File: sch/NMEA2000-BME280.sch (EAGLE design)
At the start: 5 parts, among them IC1 5V

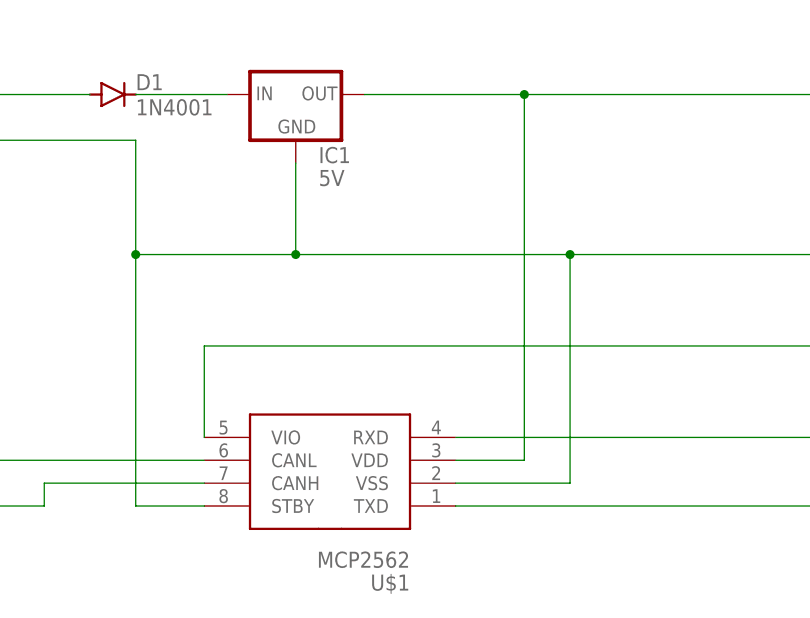
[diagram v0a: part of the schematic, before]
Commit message: added some missing values
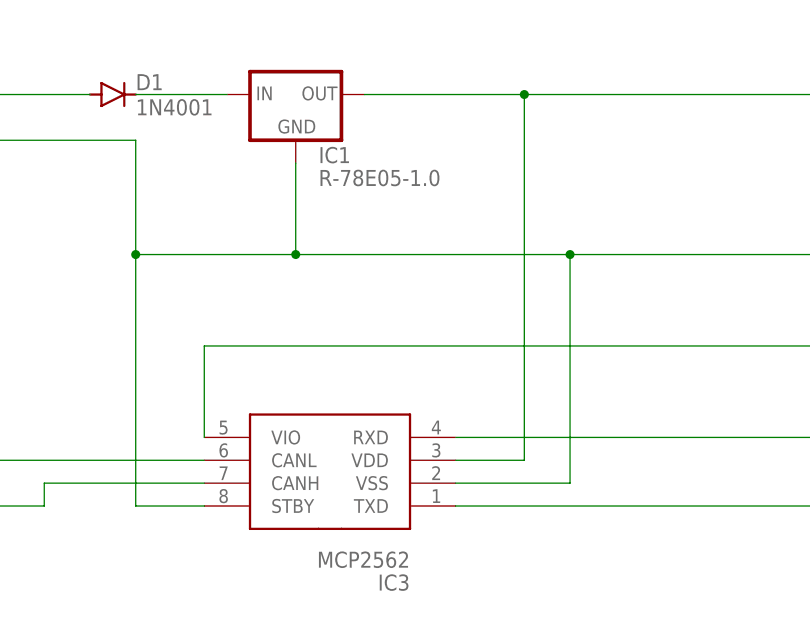
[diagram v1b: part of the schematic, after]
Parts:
- IC1: value 5V -> R-78E05-1.0
- renumbered U$1 to IC3
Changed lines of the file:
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@@
 <parts>
 <part name="ESP1" library="_esp32" deviceset="ESP32-NODEMCU" device="" value="ESP32 NodeMCU"/>
-<part name="IC1" library="v-reg" library_urn="urn:adsk.eagle:library:409" deviceset="78XXS" device="" package3d_urn="urn:adsk.eagle:package:30342/1" value="5V"/>
-<part name="U$1" library="_eigene" deviceset="MCP2562" device=""/>
+<part name="IC1" library="v-reg" library_urn="urn:adsk.eagle:library:409" deviceset="78XXS" device="" package3d_urn="urn:adsk.eagle:package:30342/1" value="R-78E05-1.0"/>
+<part name="IC3" library="_eigene" deviceset="MCP2562" device=""/>
 <part name="FRAME1" library="frames" library_urn="urn:adsk.eagle:library:229" deviceset="DINA4_L" device=""/>
 <part name="D1" library="diode" library_urn="urn:adsk.eagle:library:210" deviceset="1N4004" device="" package3d_urn="urn:adsk.eagle:package:43336/1" value="1N4001"/>
@@
 <attribute name="VALUE" x="81.28" y="83.82" size="1.778" layer="96"/>
 </instance>
-<instance part="U$1" gate="G$1" x="81.28" y="68.58" smashed="yes" rot="R180">
+<instance part="IC3" gate="G$1" x="81.28" y="68.58" smashed="yes" rot="R180">
 <attribute name="NAME" x="91.44" y="40.64" size="1.778" layer="95" rot="R180"/>
 <attribute name="VALUE" x="91.44" y="43.18" size="1.778" layer="96" rot="R180"/>
@@
 <segment>
 <wire x1="223.52" y1="109.22" x2="223.52" y2="55.88" width="0.1524" layer="91"/>
-<pinref part="U$1" gate="G$1" pin="RXD"/>
+<pinref part="IC3" gate="G$1" pin="RXD"/>
 <wire x1="223.52" y1="55.88" x2="96.52" y2="55.88" width="0.1524" layer="91"/>
 <pinref part="ESP1" gate="G$1" pin="GPIO4"/>
@@
 <net name="N$2" class="0">
 <segment>
-<pinref part="U$1" gate="G$1" pin="TXD"/>
+<pinref part="IC3" gate="G$1" pin="TXD"/>
 <wire x1="96.52" y1="48.26" x2="226.06" y2="48.26" width="0.1524" layer="91"/>
 <wire x1="226.06" y1="48.26" x2="226.06" y2="116.84" width="0.1524" layer="91"/>
@@
 <pinref part="IC1" gate="1" pin="OUT"/>
 <wire x1="162.56" y1="93.98" x2="104.14" y2="93.98" width="0.1524" layer="91"/>
-<pinref part="U$1" gate="G$1" pin="VDD"/>
+<pinref part="IC3" gate="G$1" pin="VDD"/>
 <wire x1="104.14" y1="93.98" x2="86.36" y2="93.98" width="0.1524" layer="91"/>
 <wire x1="96.52" y1="53.34" x2="104.14" y2="53.34" width="0.1524" layer="91"/>
@@
 <pinref part="ESP1" gate="G$1" pin="GND1"/>
 <wire x1="144.78" y1="106.68" x2="162.56" y2="106.68" width="0.1524" layer="91"/>
-<pinref part="U$1" gate="G$1" pin="VSS"/>
+<pinref part="IC3" gate="G$1" pin="VSS"/>
 <wire x1="96.52" y1="50.8" x2="109.22" y2="50.8" width="0.1524" layer="91"/>
 <wire x1="109.22" y1="50.8" x2="109.22" y2="76.2" width="0.1524" layer="91"/>
 <junction x="109.22" y="76.2"/>
 <label x="35.56" y="88.9" size="1.778" layer="95"/>
-<pinref part="U$1" gate="G$1" pin="STBY"/>
+<pinref part="IC3" gate="G$1" pin="STBY"/>
 <wire x1="68.58" y1="48.26" x2="60.96" y2="48.26" width="0.1524" layer="91"/>
 <wire x1="60.96" y1="76.2" x2="60.96" y2="48.26" width="0.1524" layer="91"/>
@@
 <net name="CANL" class="0">
 <segment>
-<pinref part="U$1" gate="G$1" pin="CANL"/>
+<pinref part="IC3" gate="G$1" pin="CANL"/>
 <wire x1="68.58" y1="53.34" x2="33.02" y2="53.34" width="0.1524" layer="91"/>
 <label x="35.56" y="53.34" size="1.778" layer="95"/>
@@
 <net name="CANH" class="0">
 <segment>
-<pinref part="U$1" gate="G$1" pin="CANH"/>
+<pinref part="IC3" gate="G$1" pin="CANH"/>
 <wire x1="68.58" y1="50.8" x2="50.8" y2="50.8" width="0.1524" layer="91"/>
 <label x="35.56" y="48.26" size="1.778" layer="95"/>
@@
 <segment>
 <label x="76.2" y="139.7" size="1.778" layer="95"/>
-<pinref part="U$1" gate="G$1" pin="VIO"/>
+<pinref part="IC3" gate="G$1" pin="VIO"/>
 <wire x1="139.7" y1="66.04" x2="68.58" y2="66.04" width="0.1524" layer="91"/>
 <wire x1="68.58" y1="66.04" x2="68.58" y2="55.88" width="0.1524" layer="91"/>
